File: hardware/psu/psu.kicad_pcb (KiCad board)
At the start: 2 copper layers, 165.1 x 88.9 mm, 58 parts, among them J1 Conn_01x02, J2 Conn_01x05, J3 Conn_01x02, J4 Conn_01x06, J5 Conn_01x03, J6 Conn_01x05, J7 Conn_01x08, J8 Conn_01x03, J9 Conn_01x04, SW1 SW_SPST, U1 LM7805_TO220, U2 BA33BC0T

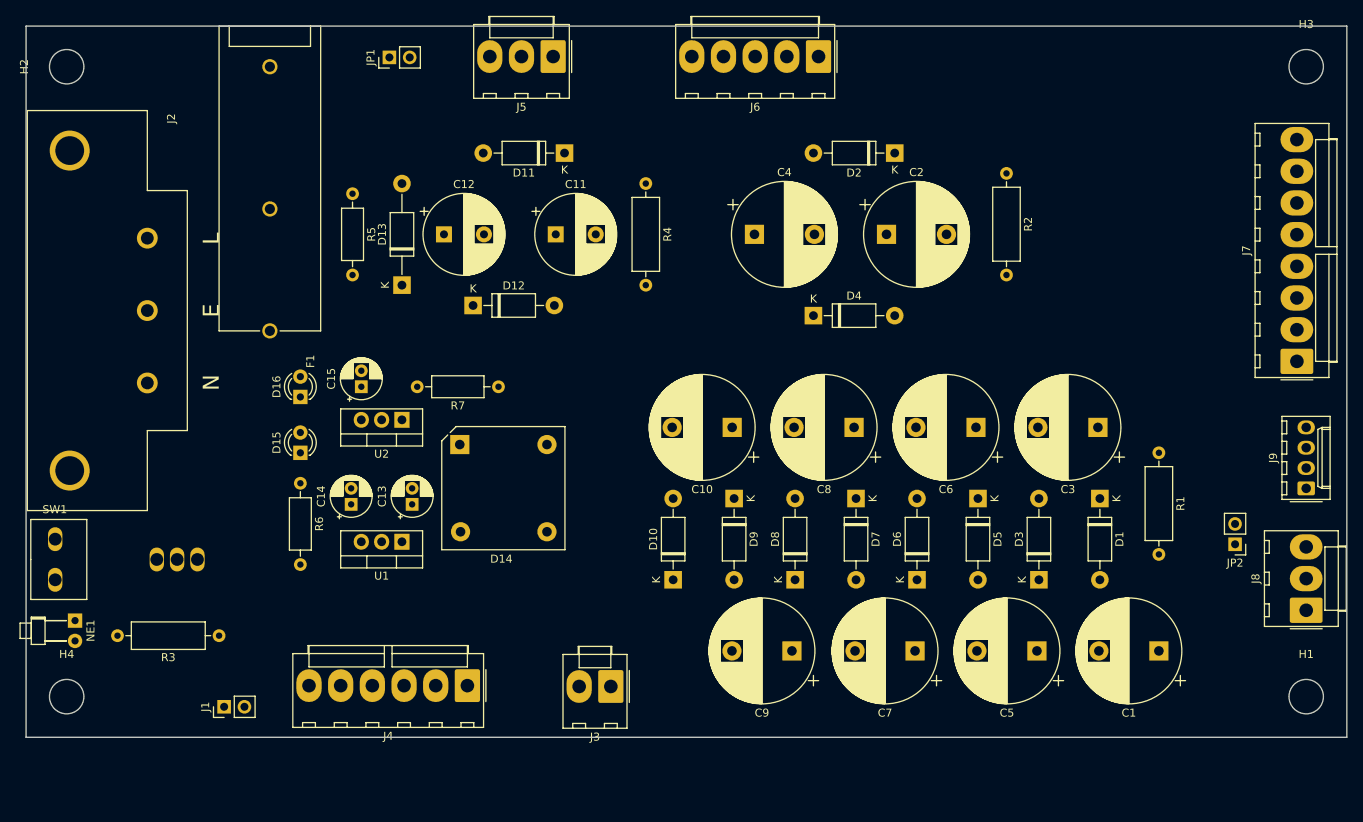
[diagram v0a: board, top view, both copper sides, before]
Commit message: rework power supply, still needs footprint/placement work
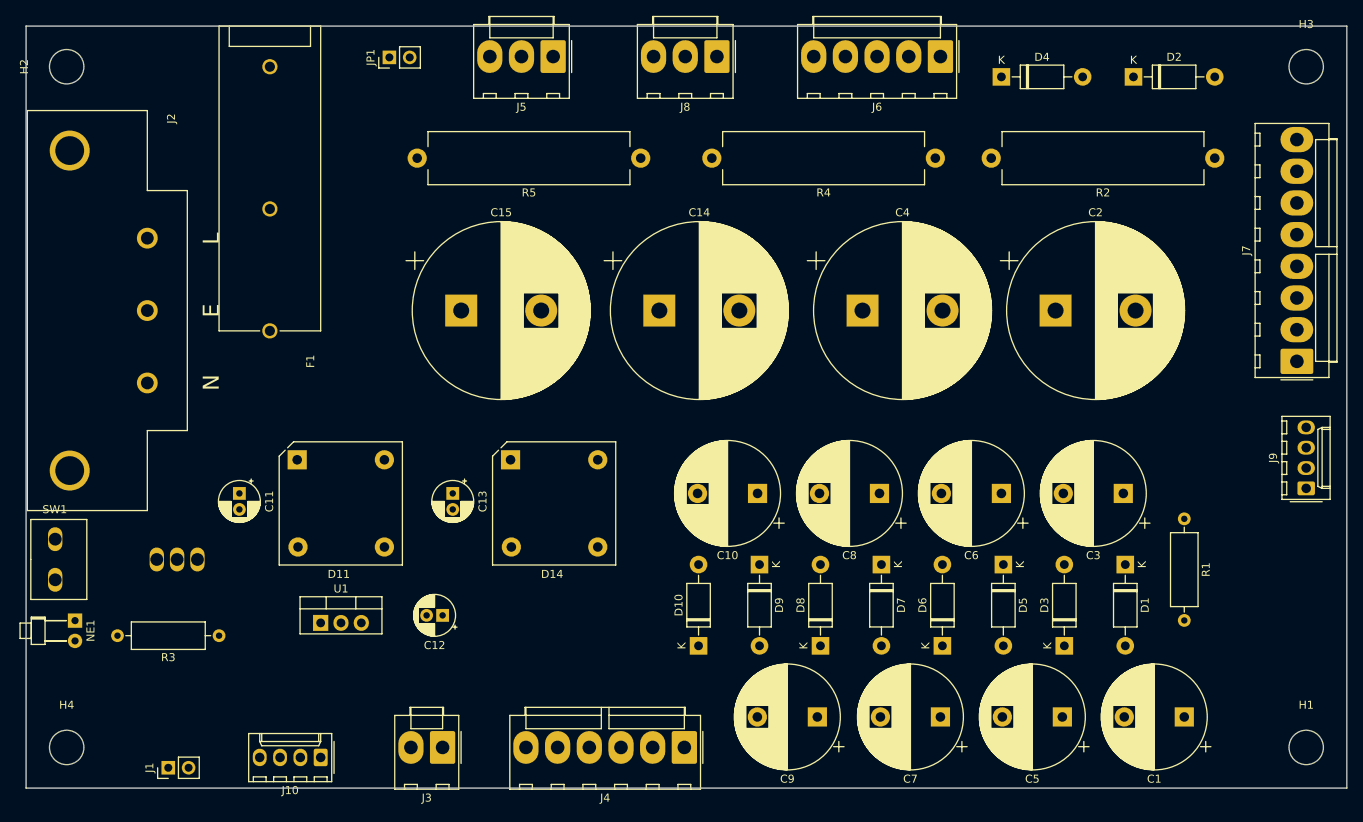
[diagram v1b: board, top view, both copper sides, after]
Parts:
- removed D12: 1N4007, Diode_THT:D_DO-41_SOD81_P10.16mm_Horizontal
- removed D13: 1N5386BG, Diode_THT:D_DO-41_SOD81_P12.70mm_Horizontal
- removed D15, D16: LED, LED_THT:LED_D3.0mm
- removed JP2: Jumper_2_Open, Connector_PinHeader_2.54mm:PinHeader_1x02_P2.54mm_Vertical
- removed R6: 1.2k, Resistor_THT:R_Axial_DIN0207_L6.3mm_D2.5mm_P10.16mm_Horizontal
- removed R7: 650, Resistor_THT:R_Axial_DIN0207_L6.3mm_D2.5mm_P10.16mm_Horizontal
- removed U2: BA33BC0T, Package_TO_SOT_THT:TO-220-3_Vertical
- added J10: Conn_01x04, Connector_Molex:Molex_KK-254_AE-6410-04A_1x04_P2.54mm_Vertical, F.Cu at (81.3, 154.9)
- C11: value 10u 250V -> 10u 25V; footprint Capacitor_THT:CP_Radial_D10.0mm_P5.00mm -> Capacitor_THT:CP_Radial_D5.0mm_P2.00mm
- C12: value 10u 250V -> 1u 10V; footprint Capacitor_THT:CP_Radial_D10.0mm_P5.00mm -> Capacitor_THT:CP_Radial_D5.0mm_P2.00mm
- C14, C15: value 1u 25V -> 100u 400V; footprint Capacitor_THT:CP_Radial_D5.0mm_P2.00mm -> Capacitor_THT:CP_Radial_D22.0mm_P10.00mm_SnapIn
- C2, C4: value 47u 400V -> 100u 400V; footprint Capacitor_THT:CP_Radial_D13.0mm_P7.50mm -> Capacitor_THT:CP_Radial_D22.0mm_P10.00mm_SnapIn
- D11: value 1N4007 -> D_Bridge_+-AA; footprint Diode_THT:D_DO-41_SOD81_P10.16mm_Horizontal -> Diode_THT:Diode_Bridge_15.1x15.1x6.3mm_P10.9mm
- R2: value 100 ohm 1/2W -> 120 ohm 5W; footprint Resistor_THT:R_Axial_DIN0309_L9.0mm_D3.2mm_P12.70mm_Horizontal -> Resistor_THT:R_Axial_Power_L25.0mm_W6.4mm_P27.94mm
- R4: value 100 ohm 1/2W -> 200 ohm 5W; footprint Resistor_THT:R_Axial_DIN0309_L9.0mm_D3.2mm_P12.70mm_Horizontal -> Resistor_THT:R_Axial_Power_L25.0mm_W6.4mm_P27.94mm
- R5: value 2.6k ohm 2W -> 200 ohm 5W; footprint Resistor_THT:R_Axial_DIN0207_L6.3mm_D2.5mm_P10.16mm_Horizontal -> Resistor_THT:R_Axial_Power_L25.0mm_W6.4mm_P27.94mm
- U1: value LM7805_TO220 -> LM7905_TO220
- moved J8 101.1 mm to (130.8, 67.3), turned to 180 degrees
- moved C11 51.1 mm to (71.1, 121.9), turned to -90 degrees
- moved D11 50.9 mm to (78.3, 117.7), turned to 0 degrees
- moved C12 47.6 mm to (96.5, 137.2), turned to 180 degrees
- moved C14 45.5 mm to (123.6, 99.1), turned to 0 degrees
- moved D4 38.0 mm to (166.4, 69.8)
- moved R4 36.3 mm to (158.1, 80.0), turned to 180 degrees
- moved R5 36.3 mm to (121.3, 80.0), turned to 180 degrees
- moved D2 31.3 mm to (182.9, 69.8), turned to 0 degrees
- moved J4 28.2 mm to (126.7, 153.7)
- moved R2 26.1 mm to (193.0, 80.0), turned to 180 degrees
- moved C2 23.2 mm to (173.1, 99.1)
- moved J3 22.4 mm to (96.5, 153.7)
- moved C4 16.5 mm to (149.0, 99.1)
- moved C15 15.7 mm to (98.8, 99.1), turned to 0 degrees
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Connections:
- C11 pad 1: Net-(C11-Pad1) -> GND
- C12 pad 1: Net-(C12-Pad1) -> GND
- C12 pad 2: /115_A -> -5V
- C13 pad 1: Net-(C13-Pad1) -> +9V
- C14 pad 1: +5V -> Net-(C14-Pad1)
- C14 pad 2: GND -> /175_2B
- C15 pad 1: +3.3V -> /+360
- C15 pad 2: GND -> /175_2B
- C3 pad 1: /0V -> /175_2B
- C4 pad 1: /+360 -> Net-(C4-Pad1)
- C4 pad 2: /0V -> /175_2B
- D1 pad 1: /0V -> /175_2B
- D11 pad 1: Net-(C11-Pad1) -> GND
- D11 pad 2: /115_A -> Net-(C11-Pad2)
- D14 pad 1: Net-(C13-Pad1) -> +9V
- D14 pad 3: /6.3_2A -> Net-(D14-Pad3)
- D14 pad 4: /6.3_2B -> Net-(D14-Pad4)
- D2 pad 2: /0V -> /175_2B
- D4 pad 1: /+360 -> Net-(C4-Pad1)
- J3 pad 2: /0V -> /175_2B
- J4 pad 3: /0V -> /175_2B
- J7 pad 2: /0V -> /175_2B
- J7 pad 4: /0V -> /175_2B
- J8 pad 1: Net-(D13-Pad1) -> /SW_ACL
- J8 pad 2: /115_A -> /ACN
- J9 pad 1: +5V -> +9V
- J9 pad 3: +3.3V -> -5V
- JP1 pad 2: /0V -> /175_2B
- R4 pad 1: /115_B -> Net-(C4-Pad1)
- R4 pad 2: Net-(C11-Pad2) -> Net-(C14-Pad1)
- R5 pad 1: Net-(C12-Pad1) -> Net-(C14-Pad1)
- R5 pad 2: Net-(D13-Pad1) -> /+360
- U1 pad 1: Net-(C13-Pad1) -> GND
- U1 pad 2: GND -> Net-(C11-Pad2)
- U1 pad 3: +5V -> -5V
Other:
- board size 165.1 x 88.9 mm -> 165.1 x 95.2 mm

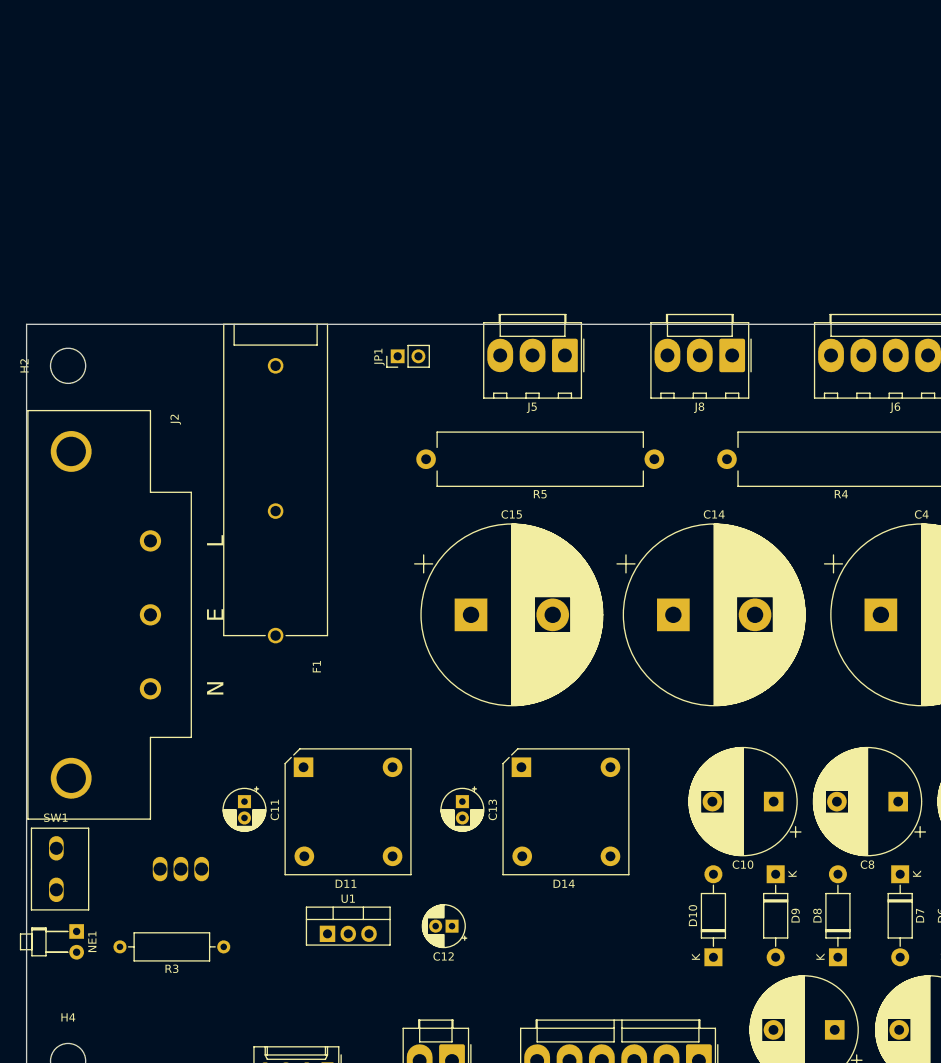
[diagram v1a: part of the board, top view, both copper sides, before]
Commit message: Add some stuff to PSU
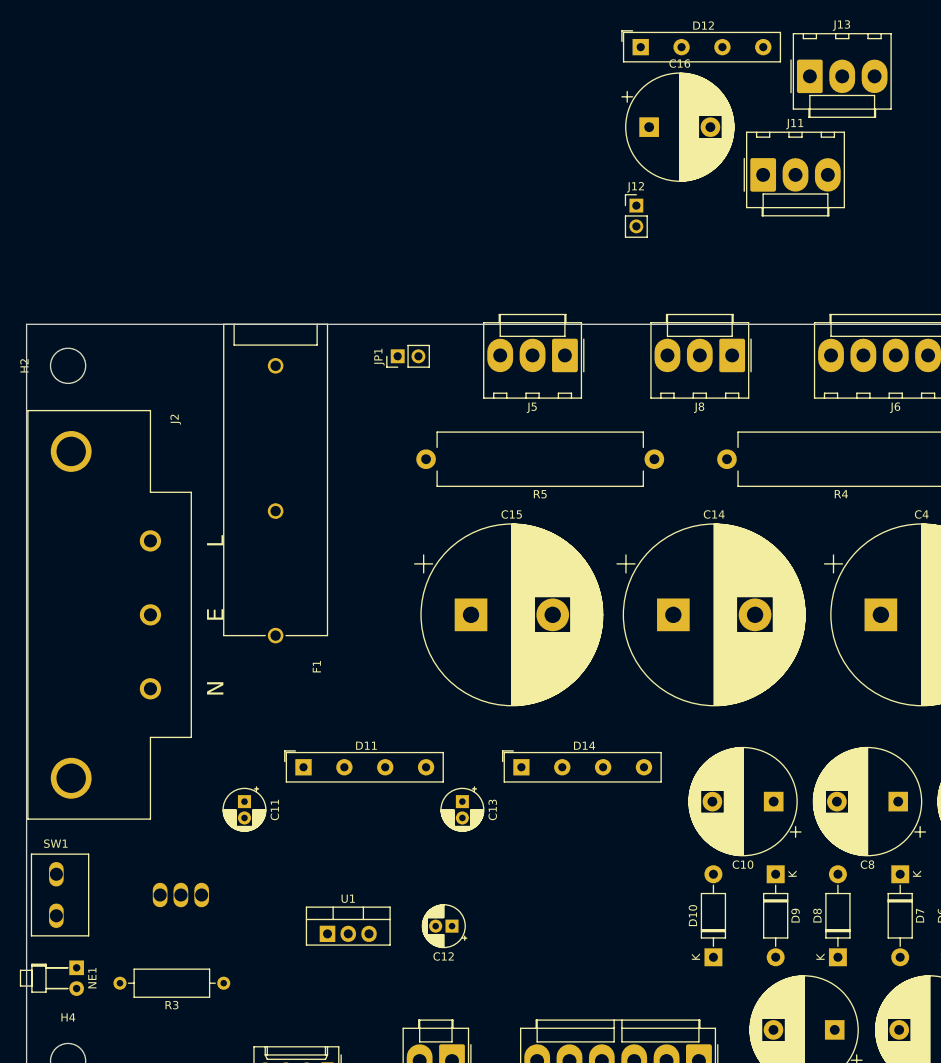
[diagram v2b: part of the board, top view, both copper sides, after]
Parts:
- added C16: 47u 400V, Capacitor_THT:CP_Radial_D13.0mm_P7.50mm, F.Cu at (120.7, 39.4)
- added D12: D_Bridge_+-AA, Diode_THT:Diode_Bridge_19.0x3.5x10.0mm_P5.0mm, F.Cu at (119.6, 29.6)
- added J11: Conn_01x03, Connector_Molex:Molex_KK-396_A-41791-0003_1x03_P3.96mm_Vertical, F.Cu at (134.6, 45.2)
- added J12: Conn_01x02, Connector_PinHeader_2.54mm:PinHeader_1x02_P2.54mm_Vertical, F.Cu at (119.1, 49.0)
- added J13: Conn_01x03, Connector_Molex:Molex_KK-396_A-41791-0003_1x03_P3.96mm_Vertical, F.Cu at (140.3, 33.1)
- D11, D14: footprint Diode_THT:Diode_Bridge_15.1x15.1x6.3mm_P10.9mm -> Diode_THT:Diode_Bridge_19.0x3.5x10.0mm_P5.0mm
- moved R3 4.45 mm to (68.6, 144.1)
- moved NE1 4.44 mm to (50.6, 142.3)
- moved SW1 3.17 mm to (60.8, 133.3)
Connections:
- net /175_2B renamed /0V
- C11 pad 1: GND -> -5V
- C12 pad 1: GND -> -5V
- C13 pad 2: GND -> -5V
- D11 pad 1: GND -> -5V
- D11 pad 2: Net-(C11-Pad2) -> Net-(D11-Pad2)
- D11 pad 4: Net-(D11-Pad4) -> Net-(C11-Pad2)
- D14 pad 2: GND -> Net-(D14-Pad2)
- D14 pad 4: Net-(D14-Pad4) -> -5V
- J10 pad 1: Net-(D14-Pad3) -> Net-(D14-Pad2)
- J10 pad 2: Net-(D14-Pad4) -> Net-(D14-Pad3)
- J10 pad 3: Net-(D11-Pad3) -> Net-(D11-Pad2)
- J10 pad 4: Net-(D11-Pad4) -> Net-(D11-Pad3)
- J2 pad 2: GND -> -5V
- J2 pad 4: GND -> -5V
- J2 pad 5: GND -> -5V
- J5 pad 3: GND -> -5V
- J6 pad 5: GND -> -5V
- J8 pad 3: GND -> -5V
- J9 pad 2: GND -> -5V
- J9 pad 4: GND -> -5V
- JP1 pad 1: GND -> -5V
- U1 pad 1: GND -> -5V

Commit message: working on chassis layout
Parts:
- moved J3 153.7 mm to (186.7, 29.2)
- moved J1 142.3 mm to (200.7, 123.2), turned to 180 degrees
- moved J13 118.2 mm to (79.9, 134.7)
- moved J8 96.3 mm to (62.1, 134.7), turned to 0 degrees
- moved J5 94.4 mm to (44.3, 134.7), turned to 0 degrees
- moved J11 93.1 mm to (198.2, 113.2), turned to 90 degrees
- moved R3 90.3 mm to (49.5, 55.9)
- moved NE1 90.3 mm to (31.5, 54.0)
- moved C16 84.7 mm to (88.9, 117.9), turned to 90 degrees
- moved J9 79.9 mm to (125.7, 134.6), turned to 0 degrees
- moved D12 71.2 mm to (88.9, 93.8), turned to 90 degrees
- moved SW1 70.0 mm to (41.7, 66.0)
- moved J4 59.3 mm to (182.9, 134.6)
- moved F1 58.4 mm to (63.1, 44.5), turned to 0 degrees
- moved J6 47.8 mm to (198.2, 94.3), turned to 90 degrees
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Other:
- board size 165.1 x 95.2 mm -> 177.8 x 114.3 mm

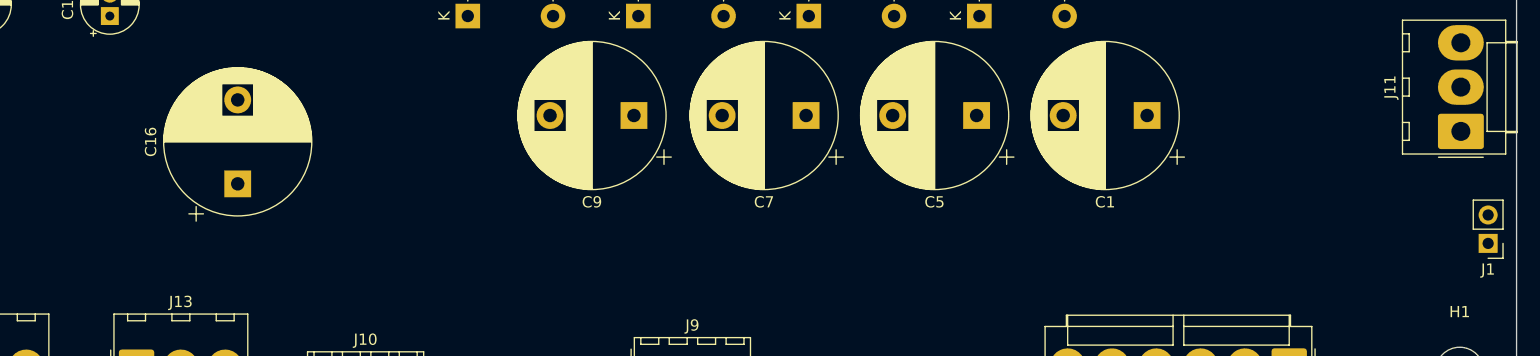
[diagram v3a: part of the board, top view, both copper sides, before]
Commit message: Add CRT voltage select jumper
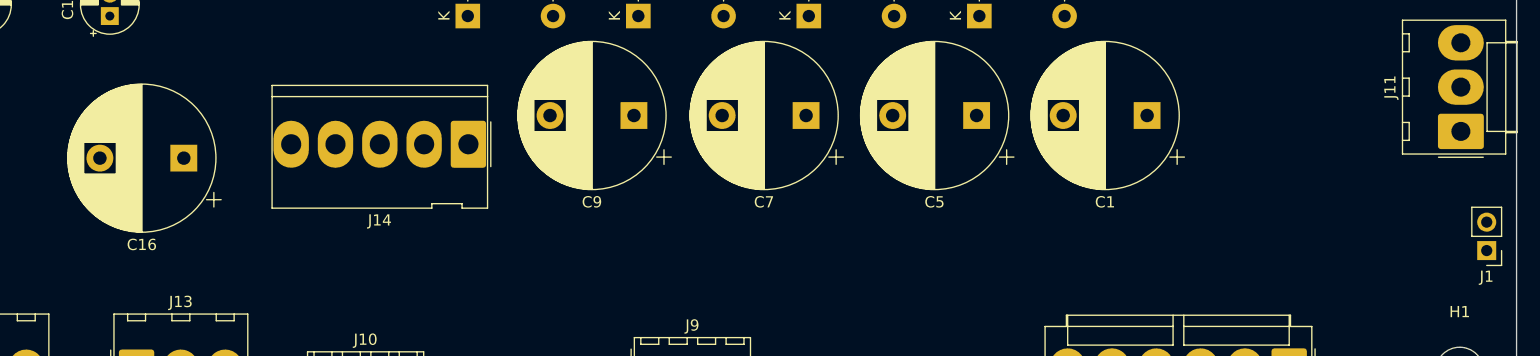
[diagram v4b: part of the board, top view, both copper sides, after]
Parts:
- added J14: Conn_01x05, Connector_Molex:Molex_KK-396_5273-05A_1x05_P3.96mm_Vertical, F.Cu at (109.5, 114.3)
- moved C16 5.34 mm to (84.1, 115.6), turned to 180 degrees
- moved J1 0.65 mm to (200.5, 123.8)
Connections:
- net Net-(C10-Pad1) renamed /S5
- net Net-(C7-Pad2) renamed /S4
- net Net-(C9-Pad2) renamed /S6
- C10 pad 2: /-1400 -> /S7
- D10 pad 2: /-1400 -> /S7
- J4 pad 6: /-1400 -> /-V_CRT

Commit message: working on PSU
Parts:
- added J15: Conn_01x02, Connector_PinHeader_2.54mm:PinHeader_1x02_P2.54mm_Vertical, F.Cu at (259.1, 36.8)
- added K1: PR16-12V-540-2C, my_relay:DIP-22_W7.62mm_LongPads, F.Cu at (184.2, 74.9)
- added Q1: Q_NMOS_GDS, Package_TO_SOT_THT:TO-220-3_Vertical, F.Cu at (248.4, 38.4)
- added R10: 1.0M 2W, Resistor_THT:R_Axial_DIN0309_L9.0mm_D3.2mm_P15.24mm_Horizontal, F.Cu at (215.0, 63.9)
- added R11: 1.0M 2W, Resistor_THT:R_Axial_DIN0309_L9.0mm_D3.2mm_P15.24mm_Horizontal, F.Cu at (246.8, 32.1)
- added R6: 1.0M 2W, Resistor_THT:R_Axial_DIN0309_L9.0mm_D3.2mm_P15.24mm_Horizontal, F.Cu at (212.1, 88.9)
- added R7: 1.0M 2W, Resistor_THT:R_Axial_DIN0309_L9.0mm_D3.2mm_P15.24mm_Horizontal, F.Cu at (212.1, 74.7)
- added R8: 1.0M 2W, Resistor_THT:R_Axial_DIN0309_L9.0mm_D3.2mm_P15.24mm_Horizontal, F.Cu at (212.1, 84.2)
- added R9: 1.0M 2W, Resistor_THT:R_Axial_DIN0309_L9.0mm_D3.2mm_P15.24mm_Horizontal, F.Cu at (212.1, 79.4)
- C1, C10, C16, C3, C5, C6, C7, C8, C9: footprint Capacitor_THT:CP_Radial_D13.0mm_P7.50mm -> Capacitor_THT:CP_Radial_D12.5mm_P5.00mm
- C12: footprint Capacitor_THT:CP_Radial_D5.0mm_P2.00mm -> Capacitor_THT:C_Disc_D5.0mm_W2.5mm_P5.00mm
- JP1: value Jumper_2_Open -> WIRE_JUMPER
- R2, R4, R5: footprint Resistor_THT:R_Axial_Power_L25.0mm_W6.4mm_P27.94mm -> Resistor_THT:R_Axial_DIN0617_L17.0mm_D6.0mm_P25.40mm_Horizontal
- moved H1 12.7 mm to (198.1, 121.9)
- moved J1 10.8 mm to (200.7, 134.6)
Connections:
- net +9V renamed +12V
- C11 pad 1: -5V -> GND
- C12 pad 1: -5V -> GND
- C13 pad 2: -5V -> GND
- D11 pad 1: -5V -> GND
- D14 pad 4: -5V -> GND
- J13 pad 3: -5V -> GND
- J2 pad 2: -5V -> GND
- J2 pad 4: -5V -> GND
- J2 pad 5: -5V -> GND
- J5 pad 3: -5V -> GND
- J6 pad 5: -5V -> GND
- J8 pad 3: -5V -> GND
- J9 pad 2: -5V -> GND
- J9 pad 3: -5V -> GND
- J9 pad 4: -5V -> GND
- JP1 pad 1: -5V -> GND
- U1 pad 1: -5V -> GND
